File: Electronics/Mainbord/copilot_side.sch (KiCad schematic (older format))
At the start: 19 parts, among them U50 74HC165, U51 74HC165, U52 74HC165, U53 74HC165, U54 4067, U55 74HC4051, U56 74HC595

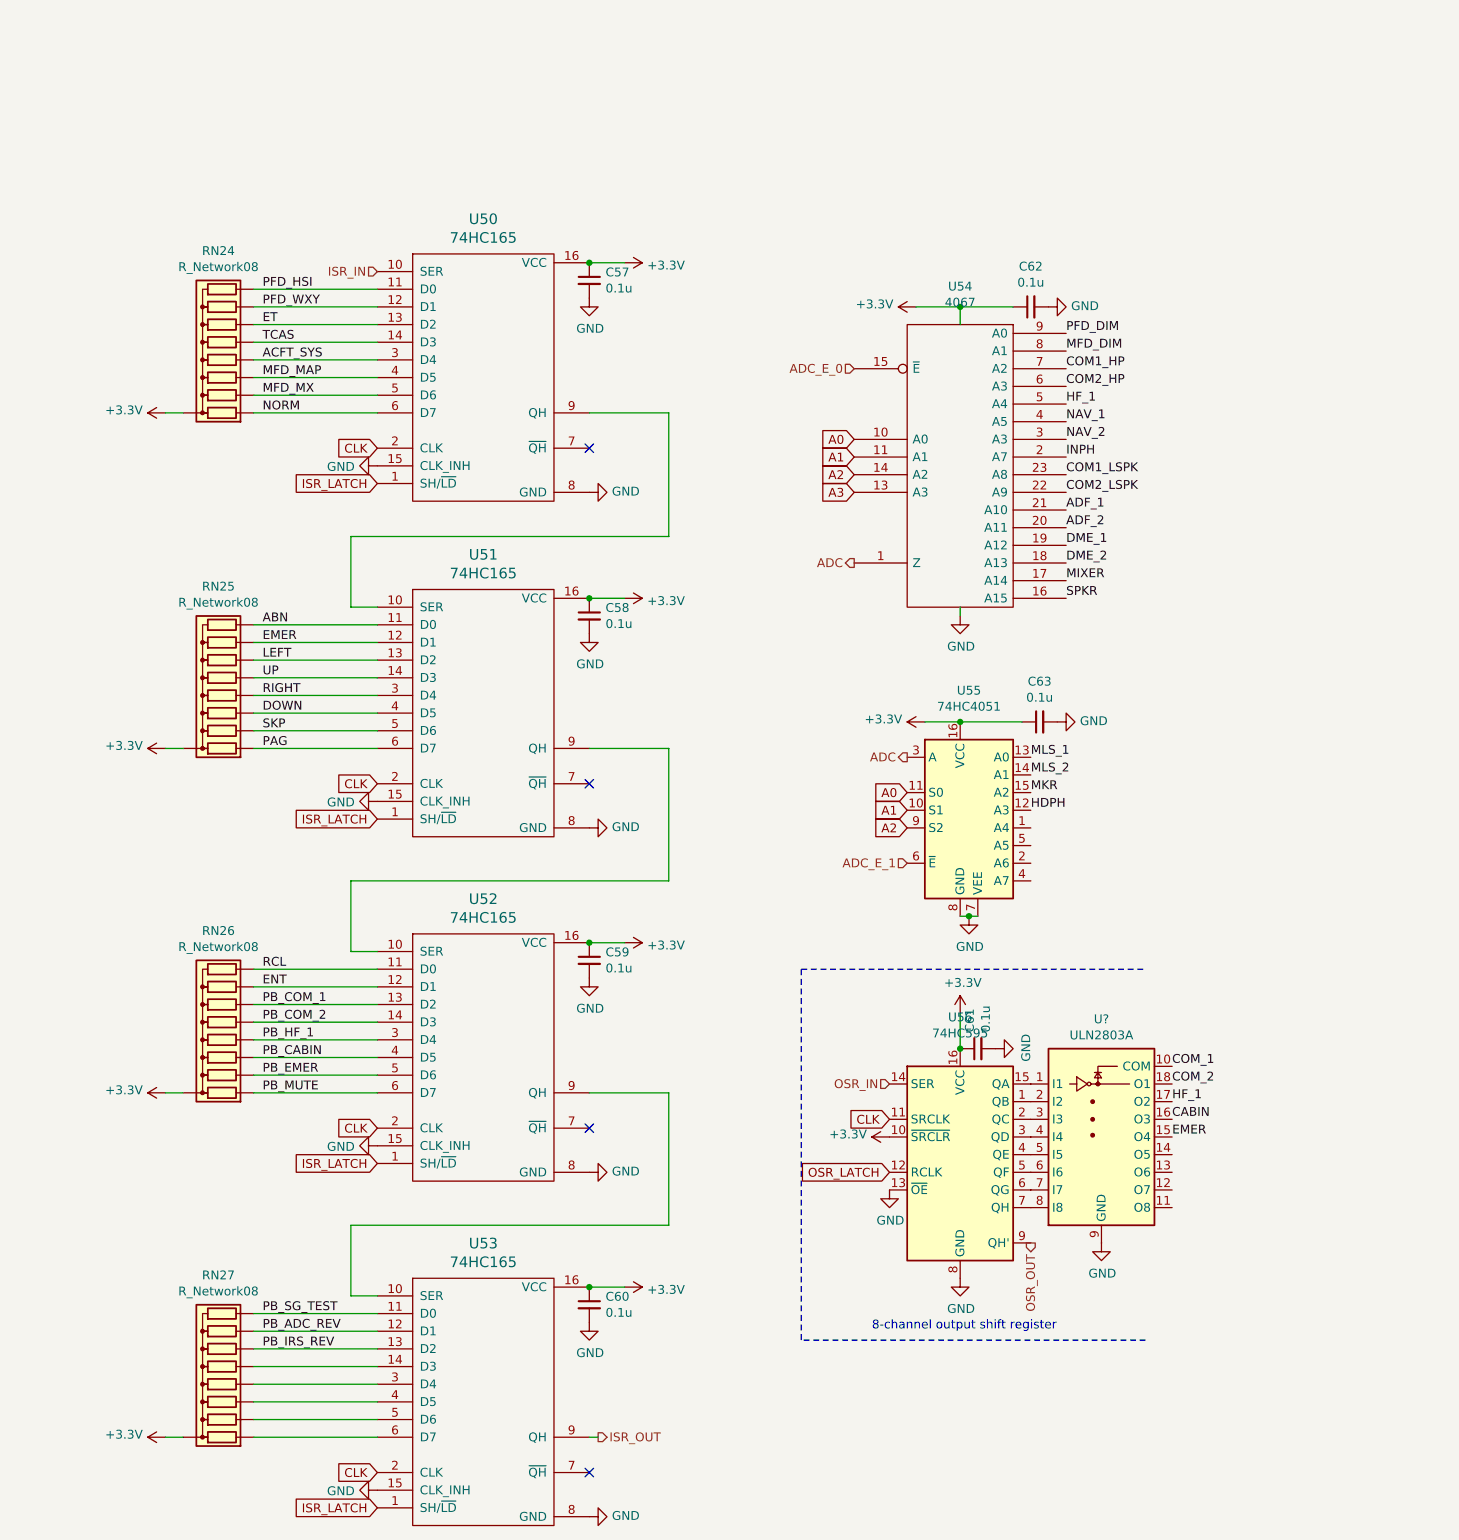
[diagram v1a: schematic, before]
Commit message: Electronics - Minor changes
Resistors to LEDs, transistors
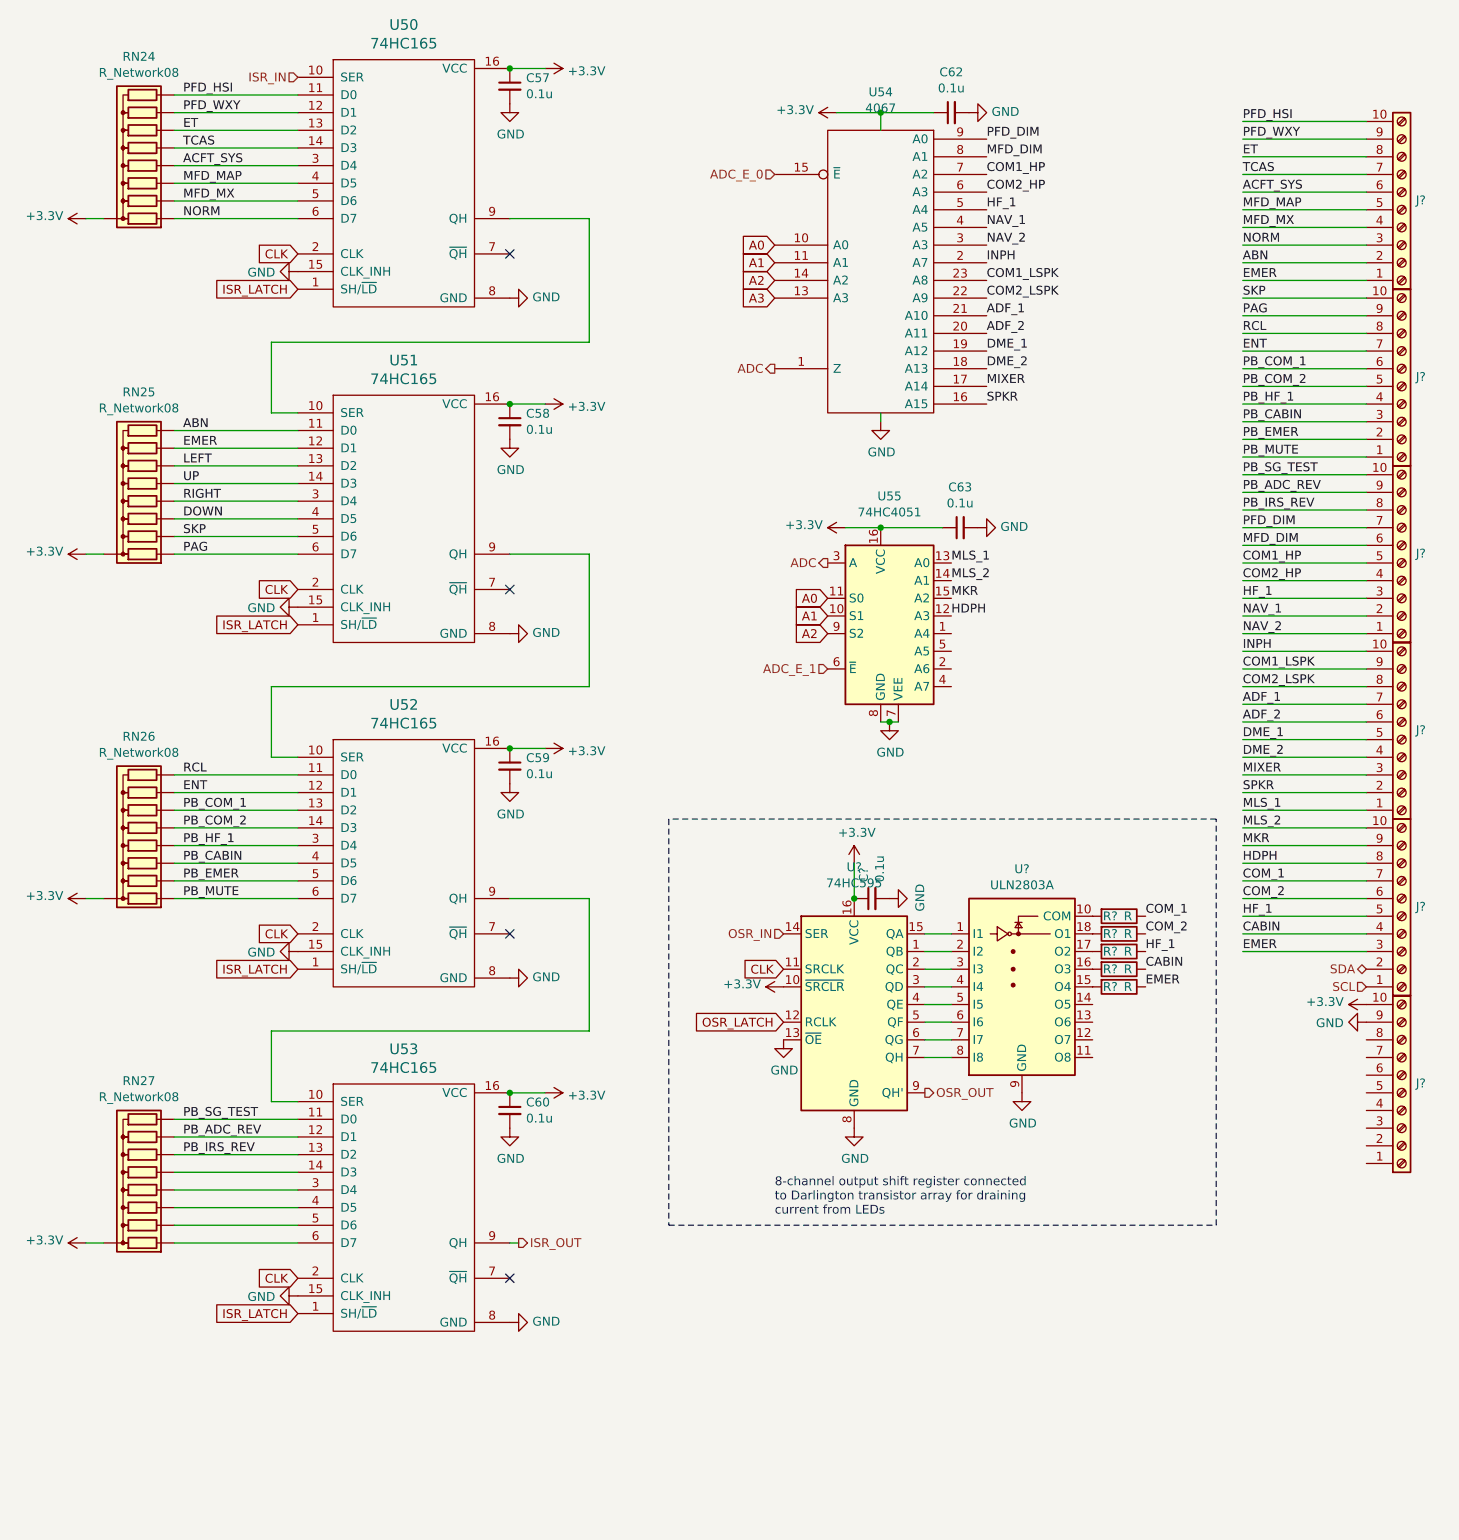
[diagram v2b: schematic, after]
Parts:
- removed C61: 0.1u, symbol Device:C_Small
- removed U56: 74HC595, symbol 74xx:74HC595
- removed U?: ULN2803A, symbol Transistor_Array:ULN2803A
- added C?: 0.1u, symbol Device:C_Small
- added J? (x6): Screw_Terminal_01x10, symbol Connector:Screw_Terminal_01x10
- added R? (x5): R, symbol Device:R
- added U?: 74HC595, symbol 74xx:74HC595
- added U?: ULN2803A, symbol Transistor_Array:ULN2803A
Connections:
- net +3V3: now also C?.1, J?.10 (Pin_10), U?.10 (~SRCLR), U?.16 (VCC)
- net ABN: now also J?.2 (Pin_2)
- net ACFT_SYS: now also J?.6 (Pin_6)
- net ADF_1: now also J?.7 (Pin_7)
- net ADF_2: now also J?.6 (Pin_6)
- net CABIN: now also J?.4 (Pin_4), R?.1
- net CLK: now also U?.11 (SRCLK)
- net COM1_HP: now also J?.5 (Pin_5)
- net COM1_LSPK: now also J?.9 (Pin_9)
- net COM2_HP: now also J?.4 (Pin_4)
- net COM2_LSPK: now also J?.8 (Pin_8)
- net COM_1: now also J?.7 (Pin_7), R?.1
- net COM_2: now also J?.6 (Pin_6), R?.1
- net DME_1: now also J?.5 (Pin_5)
- net DME_2: now also J?.4 (Pin_4)
- net EMER: now also J?.1 (Pin_1), J?.3 (Pin_3), R?.1
- net ENT: now also J?.7 (Pin_7)
- net ET: now also J?.8 (Pin_8)
- net GND: now also C?.2, J?.9 (Pin_9), U?.13 (~OE), U?.8 (GND), U?.9 (GND)
- net HDPH: now also J?.8 (Pin_8)
- net HF_1: now also J?.3 (Pin_3), J?.5 (Pin_5), R?.1
- net INPH: now also J?.10 (Pin_10)
- net MFD_DIM: now also J?.6 (Pin_6)
- net MFD_MAP: now also J?.5 (Pin_5)
- net MFD_MX: now also J?.4 (Pin_4)
- net MIXER: now also J?.3 (Pin_3)
- net MKR: now also J?.9 (Pin_9)
- net MLS_1: now also J?.1 (Pin_1)
- net MLS_2: now also J?.10 (Pin_10)
- net NAV_1: now also J?.2 (Pin_2)
- net NAV_2: now also J?.1 (Pin_1)
- net NORM: now also J?.3 (Pin_3)
- net OSR_IN: now also U?.14 (SER)
- net OSR_LATCH: now also U?.12 (RCLK)
- net OSR_OUT: now also U?.9 (QH')
- net PAG: now also J?.9 (Pin_9)
- net PB_ADC_REV: now also J?.9 (Pin_9)
- net PB_CABIN: now also J?.3 (Pin_3)
- net PB_COM_1: now also J?.6 (Pin_6)
- net PB_COM_2: now also J?.5 (Pin_5)
- net PB_EMER: now also J?.2 (Pin_2)
- net PB_HF_1: now also J?.4 (Pin_4)
- net PB_IRS_REV: now also J?.8 (Pin_8)
- net PB_MUTE: now also J?.1 (Pin_1)
- net PB_SG_TEST: now also J?.10 (Pin_10)
- net PFD_DIM: now also J?.7 (Pin_7)
- net PFD_HSI: now also J?.10 (Pin_10)
- net PFD_WXY: now also J?.9 (Pin_9)
- net RCL: now also J?.8 (Pin_8)
- net SKP: now also J?.10 (Pin_10)
- net SPKR: now also J?.2 (Pin_2)
- net TCAS: now also J?.7 (Pin_7)
- new net: U?.1 (QB), U?.2 (I2)
- new net: U?.1 (I1), U?.15 (QA)
- new net: U?.2 (QC), U?.3 (I3)
- new net: U?.3 (QD), U?.4 (I4)
- new net: U?.4 (QE), U?.5 (I5)
- new net: U?.5 (QF), U?.6 (I6)
- new net: U?.6 (QG), U?.7 (I7)
- new net: U?.7 (QH), U?.8 (I8)
- new net: R?.2, U?.10 (COM)
- new net: R?.2, U?.15 (O4)
- new net: R?.2, U?.16 (O3)
- new net: R?.2, U?.17 (O2)
- new net: R?.2, U?.18 (O1)
- new net SCL: J?.1 (Pin_1)
- new net SDA: J?.2 (Pin_2)
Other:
- note added: "8-channel output shift register connected \nto Darlington transistor array for draining \ncurrent from LEDs"
- note removed: "8-channel output shift register"
- moved on the sheet: C57, C58, C59, C60, C62, C63, RN24, RN25, RN26, RN27, U50, U51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
